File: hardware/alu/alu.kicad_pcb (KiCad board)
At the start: 4 copper layers, 50 x 50 mm, 70 parts, among them J1 Conn_ALU, J2 Conn_Power, U1 74LVC1G02, U10 74AUC2G04, U11 74HC4017, U12 74LVC1G157, U13 74HC595, U14 74HC86, U15 74LVC1G32, U16 74LVC1G08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

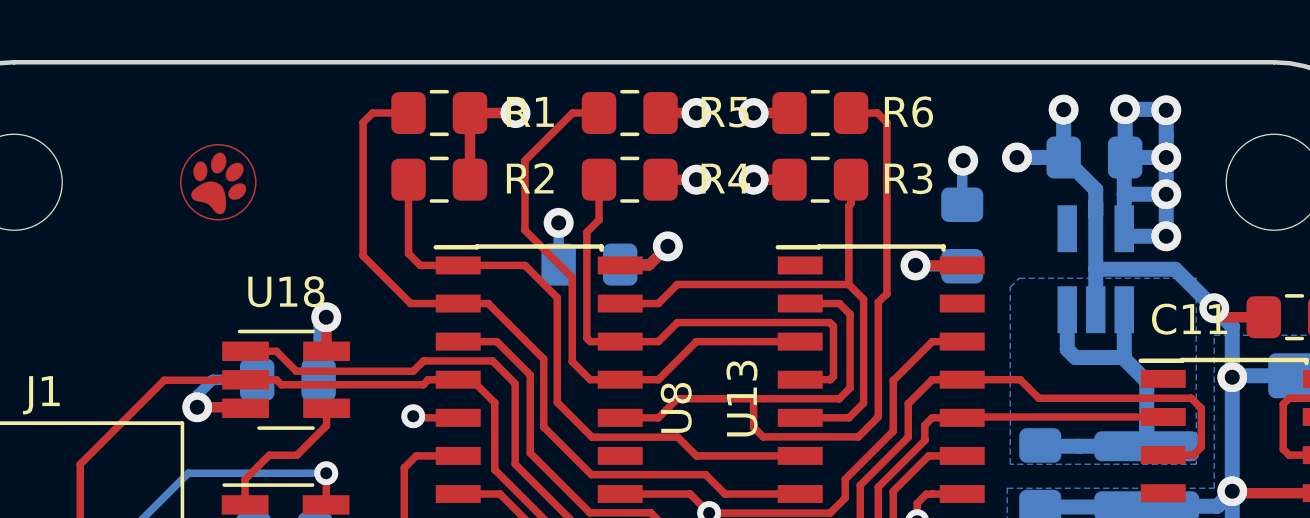
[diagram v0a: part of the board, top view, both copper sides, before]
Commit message: Added test points
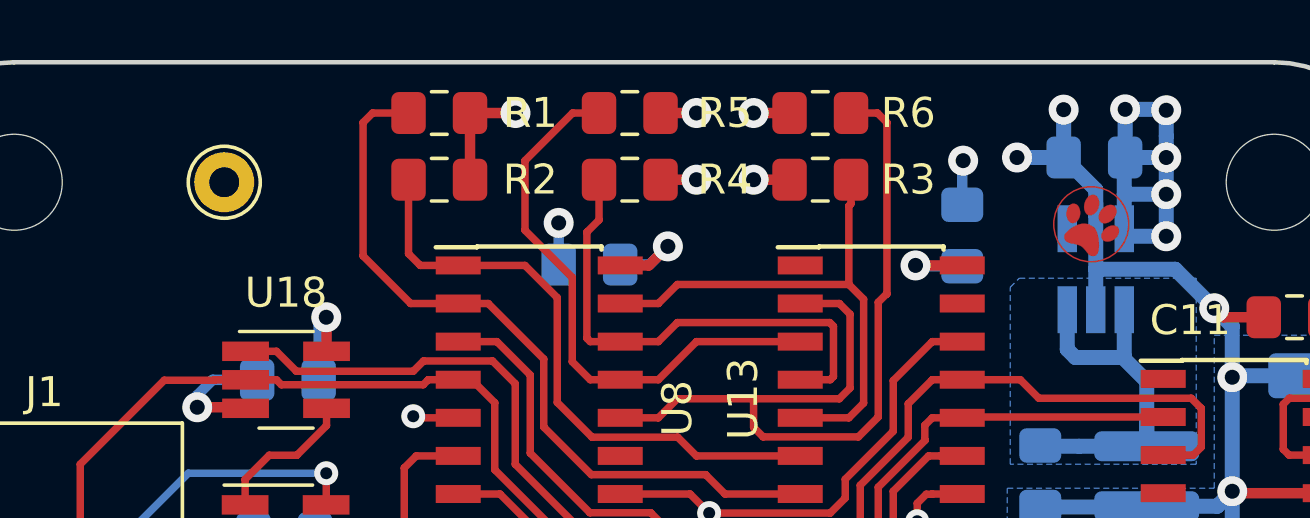
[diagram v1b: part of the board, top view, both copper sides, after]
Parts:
- added TP1: TestPoint, TestPoint:TestPoint_THTPad_D2.0mm_Drill1.0mm, F.Cu at (63.0, 82.0)
- moved G*** 29.1 mm to (91.9, 83.4)
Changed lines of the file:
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@@
     (tracks 1016)
     (zones 0)
-    (modules 70)
+    (modules 71)
     (nets 80)
   )
@@
   )
   (setup
-    (last_trace_width 0.25)
+    (last_trace_width 0.35)
     (user_trace_width 0.35)
     (user_trace_width 0.5)
@@
     (mod_text_size 1 1)
     (mod_text_width 0.15)
-    (pad_size 1.15 1.4)
-    (pad_drill 0)
+    (pad_size 2 2)
+    (pad_drill 1)
     (pad_to_mask_clearance 0.051)
     (solder_mask_min_width 0.25)
@@
   )
   (module Logo:paw-cu-circ (layer F.Cu)
-    (at 62.8 82 330)
+    (at 91.9 83.4 330)
     (fp_text reference G*** (at 0 0 330) (layer F.SilkS) hide
       (effects (font (size 1.524 1.524) (thickness 0.3)))
@@
     )
   )
+  (module TestPoint:TestPoint_THTPad_D2.0mm_Drill1.0mm (layer F.Cu)
+    (at 63 82)
+    (descr "THT pad as test Point, diameter 2.0mm, hole diameter 1.0mm")
+    (tags "test point THT pad")
+    (attr virtual)
+    (fp_text reference TP1 (at 0 -1.998) (layer F.SilkS) hide
+      (effects (font (size 1 1) (thickness 0.15)))
+    )
+    (fp_text value TestPoint (at 0 2.05) (layer F.Fab)
+      (effects (font (size 1 1) (thickness 0.15)))
+    )
+    (fp_text user %R (at 0 -2) (layer F.Fab)
+      (effects (font (size 1 1) (thickness 0.15)))
+    )
+    (fp_circle (center 0 0) (end 1.5 0) (layer F.CrtYd) (width 0.05))
+    (fp_circle (center 0 0) (end 0 1.2) (layer F.SilkS) (width 0.12))
+    (pad 1 thru_hole circle (at 0 0) (size 2 2) (drill 1) (layers *.Cu *.Mask)
+      (net 1 GND))
+  )
   (gr_text JLCJLCJLCJLC (at 60.25 103 90) (layer F.SilkS)
